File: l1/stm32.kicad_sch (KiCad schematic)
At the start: 9 parts, among them J4 Conn_01x04, SW1 SW_Push, U3 STM32G031K8Tx, Y1 32KHz768

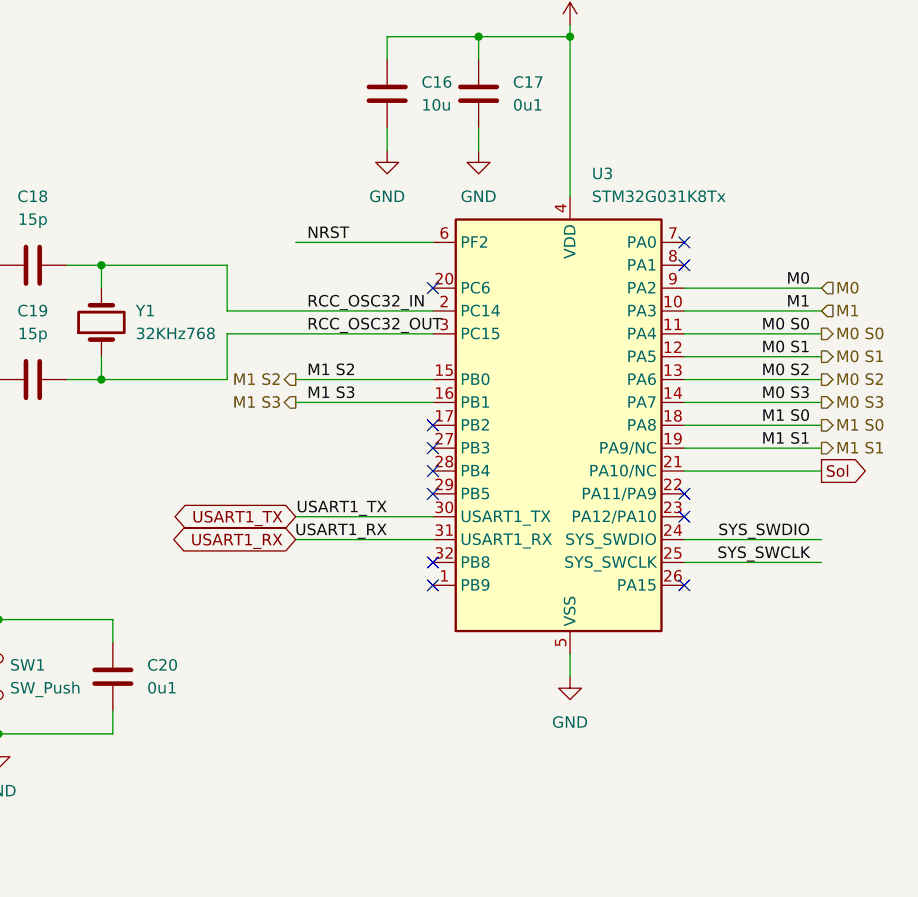
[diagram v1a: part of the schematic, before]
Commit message: Changed To G071
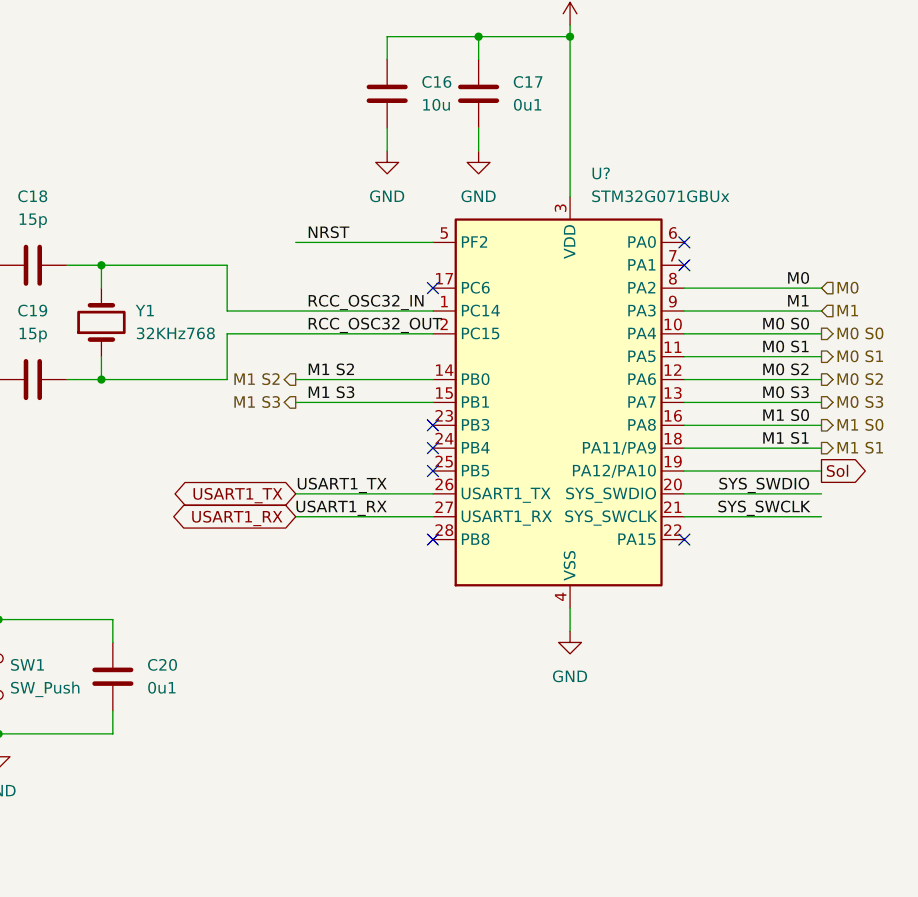
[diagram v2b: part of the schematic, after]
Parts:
- removed U3: STM32G031K8Tx, Package_QFP:LQFP-32_7x7mm_P0.8mm, symbol MCU_ST_STM32G0:STM32G031K8Tx
- added U?: STM32G071GBUx, Package_DFN_QFN:QFN-28_4x4mm_P0.5mm, symbol MCU_ST_STM32G0:STM32G071GBUx
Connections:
- net +3V3: now also U?.3 (VDD)
- net GND: now also U?.4 (VSS)
- net M0: now also U?.8 (PA2)
- net M0 S0: now also U?.10 (PA4)
- net M0 S1: now also U?.11 (PA5)
- net M0 S2: now also U?.12 (PA6)
- net M0 S3: now also U?.13 (PA7)
- net M1: now also U?.9 (PA3)
- net M1 S0: now also U?.16 (PA8)
- net M1 S1: now also U?.18 (PA11/PA9)
- net M1 S2: now also U?.14 (PB0)
- net M1 S3: now also U?.15 (PB1)
- net NRST: now also U?.5 (PF2)
- net RCC_OSC32_IN: now also U?.1 (PC14)
- net RCC_OSC32_OUT: now also U?.2 (PC15)
- net SYS_SWCLK: now also U?.21 (PA14)
- net SYS_SWDIO: now also U?.20 (PA13)
- net Sol: now also U?.19 (PA12/PA10)
- net USART1_RX: now also U?.27 (PB7)
- net USART1_TX: now also U?.26 (PB6)
- no-connect marks 12 -> 8

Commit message: Changed To OKL
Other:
- moved on the sheet: C16, C17, C18, C19, C20, SW1, U?, Y1

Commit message: rough ideation
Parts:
- gave numbers to parts that had none: 1
- renumbered C16 to C201, C17 to C202, C18 to C203, C19 to C204, C20 to C205, J4 to J201, SW1 to SW201, Y1 to Y201
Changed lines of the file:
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@@
 		(dnp no)
 		(fields_autoplaced yes)
-		(property "Reference" "Y1"
+		(property "Reference" "Y201"
 			(at 109.22 92.7099 90)
 			(effects
@@
 			(project "l1"
 				(path "/0e4ddce5-5c0a-41d1-ab67-e7bad6d98362/a63fbca6-593f-4a72-9162-84fa58a2299a/c12d892e-3e71-42fb-9089-506a5d8b9a04"
-					(reference "Y1")
+					(reference "Y201")
 					(unit 1)
 				)
@@
 		(dnp no)
 		(fields_autoplaced yes)
-		(property "Reference" "#PWR030"
+		(property "Reference" "#PWR07"
 			(at 59.69 123.19 0)
 			(effects
@@
 			(project "l1"
 				(path "/0e4ddce5-5c0a-41d1-ab67-e7bad6d98362/a63fbca6-593f-4a72-9162-84fa58a2299a/c12d892e-3e71-42fb-9089-506a5d8b9a04"
-					(reference "#PWR030")
+					(reference "#PWR07")
 					(unit 1)
 				)
@@
 		(dnp no)
 		(fields_autoplaced yes)
-		(property "Reference" "U?"
+		(property "Reference" "U201"
 			(at 159.8232 77.47 0)
 			(effects
@@
 			(project "l1"
 				(path "/0e4ddce5-5c0a-41d1-ab67-e7bad6d98362/a63fbca6-593f-4a72-9162-84fa58a2299a/c12d892e-3e71-42fb-9089-506a5d8b9a04"
-					(reference "U?")
+					(reference "U201")
 					(unit 1)
 				)
@@
 		(dnp no)
 		(fields_autoplaced yes)
-		(property "Reference" "#PWR028"
+		(property "Reference" "#PWR06"
 			(at 82.55 93.98 0)
 			(effects
@@
 			(project "l1"
 				(path "/0e4ddce5-5c0a-41d1-ab67-e7bad6d98362/a63fbca6-593f-4a72-9162-84fa58a2299a/c12d892e-3e71-42fb-9089-506a5d8b9a04"
-					(reference "#PWR028")
+					(reference "#PWR06")
 					(unit 1)
 				)
@@
 		(dnp no)
 		(fields_autoplaced yes)
-		(property "Reference" "C20"
+		(property "Reference" "C205"
 			(at 76.2 107.9499 0)
 			(effects
@@
 			(project "l1"
 				(path "/0e4ddce5-5c0a-41d1-ab67-e7bad6d98362/a63fbca6-593f-4a72-9162-84fa58a2299a/c12d892e-3e71-42fb-9089-506a5d8b9a04"
-					(reference "C20")
+					(reference "C205")
 					(unit 1)
 				)
@@
 		(dnp no)
 		(fields_autoplaced yes)
-		(property "Reference" "#PWR032"
+		(property "Reference" "#PWR010"
 			(at 60.96 157.48 0)
 			(effects
@@
 			(project "l1"
 				(path "/0e4ddce5-5c0a-41d1-ab67-e7bad6d98362/a63fbca6-593f-4a72-9162-84fa58a2299a/c12d892e-3e71-42fb-9089-506a5d8b9a04"
-					(reference "#PWR032")
+					(reference "#PWR010")
 					(unit 1)
 				)
@@
 		(dnp no)
 		(fields_autoplaced yes)
-		(property "Reference" "#PWR031"
+		(property "Reference" "#PWR09"
 			(at 60.96 142.24 0)
 			(effects
@@
 			(project "l1"
 				(path "/0e4ddce5-5c0a-41d1-ab67-e7bad6d98362/a63fbca6-593f-4a72-9162-84fa58a2299a/c12d892e-3e71-42fb-9089-506a5d8b9a04"
-					(reference "#PWR031")
+					(reference "#PWR09")
 					(unit 1)
 				)
@@
 		(dnp no)
 		(fields_autoplaced yes)
-		(property "Reference" "#PWR027"
+		(property "Reference" "#PWR05"
 			(at 147.32 81.28 0)
 			(effects
@@
 			(project "l1"
 				(path "/0e4ddce5-5c0a-41d1-ab67-e7bad6d98362/a63fbca6-593f-4a72-9162-84fa58a2299a/c12d892e-3e71-42fb-9089-506a5d8b9a04"
-					(reference "#PWR027")
+					(reference "#PWR05")
 					(unit 1)
 				)
@@
 		(dnp no)
 		(fields_autoplaced yes)
-		(property "Reference" "#PWR025"
+		(property "Reference" "#PWR03"
 			(at 157.48 64.77 0)
 			(effects
@@
 			(project "l1"
 				(path "/0e4ddce5-5c0a-41d1-ab67-e7bad6d98362/a63fbca6-593f-4a72-9162-84fa58a2299a/c12d892e-3e71-42fb-9089-506a5d8b9a04"
-					(reference "#PWR025")
+					(reference "#PWR03")
 					(unit 1)
 				)
@@
 		(dnp no)
 		(fields_autoplaced yes)
-		(property "Reference" "J4"
+		(property "Reference" "J201"
 			(at 53.34 134.62 0)
 			(effects
@@
 			(project "l1"
 				(path "/0e4ddce5-5c0a-41d1-ab67-e7bad6d98362/a63fbca6-593f-4a72-9162-84fa58a2299a/c12d892e-3e71-42fb-9089-506a5d8b9a04"
-					(reference "J4")
+					(reference "J201")
 					(unit 1)
 				)
@@
 		(dnp no)
 		(fields_autoplaced yes)
-		(property "Reference" "#PWR029"
+		(property "Reference" "#PWR08"
 			(at 157.48 134.62 0)
 			(effects
@@
 			(project "l1"
 				(path "/0e4ddce5-5c0a-41d1-ab67-e7bad6d98362/a63fbca6-593f-4a72-9162-84fa58a2299a/c12d892e-3e71-42fb-9089-506a5d8b9a04"
-					(reference "#PWR029")
+					(reference "#PWR08")
 					(unit 1)
 				)
@@
 		(dnp no)
 		(fields_autoplaced yes)
-		(property "Reference" "C16"
+		(property "Reference" "C201"
 			(at 140.97 67.3099 0)
 			(effects
@@
 			(project "l1"
 				(path "/0e4ddce5-5c0a-41d1-ab67-e7bad6d98362/a63fbca6-593f-4a72-9162-84fa58a2299a/c12d892e-3e71-42fb-9089-506a5d8b9a04"
-					(reference "C16")
+					(reference "C201")
 					(unit 1)
 				)
@@
 		(dnp no)
 		(fields_autoplaced yes)
-		(property "Reference" "C18"
+		(property "Reference" "C203"
 			(at 97.79 80.01 90)
 			(effects
@@
 			(project "l1"
 				(path "/0e4ddce5-5c0a-41d1-ab67-e7bad6d98362/a63fbca6-593f-4a72-9162-84fa58a2299a/c12d892e-3e71-42fb-9089-506a5d8b9a04"
-					(reference "C18")
+					(reference "C203")
 					(unit 1)
 				)
@@
 		(dnp no)
 		(fields_autoplaced yes)
-		(property "Reference" "SW1"
+		(property "Reference" "SW201"
 			(at 60.96 107.9499 90)
 			(effects
@@
 			(project "l1"
 				(path "/0e4ddce5-5c0a-41d1-ab67-e7bad6d98362/a63fbca6-593f-4a72-9162-84fa58a2299a/c12d892e-3e71-42fb-9089-506a5d8b9a04"
-					(reference "SW1")
+					(reference "SW201")
 					(unit 1)
 				)
@@
 		(dnp no)
 		(fields_autoplaced yes)
-		(property "Reference" "C19"
+		(property "Reference" "C204"
 			(at 97.79 92.71 90)
 			(effects
@@
 			(project "l1"
 				(path "/0e4ddce5-5c0a-41d1-ab67-e7bad6d98362/a63fbca6-593f-4a72-9162-84fa58a2299a/c12d892e-3e71-42fb-9089-506a5d8b9a04"
-					(reference "C19")
+					(reference "C204")
 					(unit 1)
 				)
@@
 		(dnp no)
 		(fields_autoplaced yes)
-		(property "Reference" "C17"
+		(property "Reference" "C202"
 			(at 151.13 67.3099 0)
 			(effects
@@
 			(project "l1"
 				(path "/0e4ddce5-5c0a-41d1-ab67-e7bad6d98362/a63fbca6-593f-4a72-9162-84fa58a2299a/c12d892e-3e71-42fb-9089-506a5d8b9a04"
-					(reference "C17")
+					(reference "C202")
 					(unit 1)
 				)
@@
 		(dnp no)
 		(fields_autoplaced yes)
-		(property "Reference" "#PWR026"
+		(property "Reference" "#PWR04"
 			(at 137.16 81.28 0)
 			(effects
@@
 			(project "l1"
 				(path "/0e4ddce5-5c0a-41d1-ab67-e7bad6d98362/a63fbca6-593f-4a72-9162-84fa58a2299a/c12d892e-3e71-42fb-9089-506a5d8b9a04"
-					(reference "#PWR026")
-					(unit 1)
-				)
+					(reference "#PWR04")
+					(unit 1)
+				)

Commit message: 死
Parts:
- removed C201: 10u, Library:cap0603, symbol Device:C
- removed C202, C205: 0u1, Library:cap0603, symbol Device:C
- removed C203, C204: 15p, Library:cap0603, symbol Device:C
- removed J201: Conn_01x04, Connector_JST:JST_XH_S4B-XH-A_1x04_P2.50mm_Horizontal, symbol Connector_Generic:Conn_01x04
- removed SW201: SW_Push, Jumper:SolderJumper-2_P1.3mm_Open_TrianglePad1.0x1.5mm, symbol Switch:SW_Push
- removed U201: STM32G071GBUx, Package_DFN_QFN:QFN-28_4x4mm_P0.5mm, symbol MCU_ST_STM32G0:STM32G071GBUx
- removed Y201: 32KHz768, Crystal:Crystal_SMD_3215-2Pin_3.2x1.5mm, symbol Device:Crystal
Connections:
- no-connect marks 8 -> 0

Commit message: 死
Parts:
- added C203: 2u2, Library:cap0603, symbol Device:C
- added C204, C205, C206, C207, C208: 0u1, Library:cap0603, symbol Device:C
- added D201: RED, Library:led0603, symbol Device:LED
- added R201: R, Library:res0603, symbol Device:R
- added R202: 1K, Library:res0603, symbol Device:R
- added U201: STM32F103CBTX, Package_QFP:LQFP-48_7x7mm_P0.5mm, symbol vincent:STM32F103CBTX
- added Y201: 8Mhz, Crystal:Resonator_SMD_Murata_CSTxExxV-3Pin_3.0x1.1mm, symbol Device:Crystal_GND3
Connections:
- new net: D201.1 (K), R202.1
- new net +3V3 FILT: C203.1, C204.1, C205.1, C206.1, C207.1, C208.1, U201.1 (VBAT), U201.24 (VDD), U201.36 (VDD), U201.48 (VDD), U201.9 (VDDA)
- new net GNDREF: C203.2, C204.2, C205.2, C206.2, C207.2, C208.2, R201.1, R202.2, U201.23 (VSS), U201.35 (VSS), U201.47 (VSS), U201.8 (VSSA), Y201.3
- new net LED DIM: U201.10 (PA0)
- new net LED RX: U201.13 (PA3)
- new net LED TX: U201.12 (PA2)
- new net M1: U201.16 (PA6)
- new net M1 S0: U201.20 (PB2)
- new net M1 S1: U201.21 (PB10)
- new net M1 S2: U201.18 (PB0)
- new net M1 S3: U201.17 (PA7)
- new net M2: U201.19 (PB1)
- new net M2 S0: U201.42 (PB6)
- new net M2 S1: U201.43 (PB7)
- new net M2 S2: U201.41 (PB5)
- new net M2 S3: U201.40 (PB4)
- new net MCU BOOT0: R201.2, U201.44 (BOOT0)
- new net MCU RST: U201.7 (NRST)
- new net MCU SWCLK: U201.37 (PA14)
- new net MCU SWDIO: U201.34 (PA13)
- new net MCU1 LED: D201.2 (A), U201.28 (PB15)
- new net MCU1 OSC IN: U201.5 (PD0), Y201.1
- new net MCU1 OSC OUT: U201.6 (PD1), Y201.2
- no-connect marks 0 -> 20

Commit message: 死
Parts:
- removed U201: STM32F103CBTX, Package_QFP:LQFP-48_7x7mm_P0.5mm, symbol vincent:STM32F103CBTX
- added U301: STM32F103CBTX, Package_DFN_QFN:QFN-48-1EP_7x7mm_P0.5mm_EP5.6x5.6mm, symbol vincent:STM32F103CBTX
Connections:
- net +3V3 FILT: now also U301.1 (VBAT), U301.24 (VDD), U301.36 (VDD), U301.48 (VDD), U301.9 (VDDA)
- net GNDREF: now also U301.23 (VSS), U301.35 (VSS), U301.47 (VSS), U301.8 (VSSA)
- net LED DIM: now also U301.10 (PA0)
- net LED RX: now also U301.13 (PA3)
- net LED TX: now also U301.12 (PA2)
- net M1: now also U301.16 (PA6)
- net M1 S0: now also U301.20 (PB2)
- net M1 S1: now also U301.21 (PB10)
- net M1 S2: now also U301.18 (PB0)
- net M1 S3: now also U301.17 (PA7)
- net M2: now also U301.19 (PB1)
- net M2 S0: now also U301.42 (PB6)
- net M2 S1: now also U301.43 (PB7)
- net M2 S2: now also U301.41 (PB5)
- net M2 S3: now also U301.40 (PB4)
- net MCU BOOT0: now also U301.44 (BOOT0)
- net MCU RST: now also U301.7 (NRST)
- net MCU SWCLK: now also U301.37 (PA14)
- net MCU SWDIO: now also U301.34 (PA13)
- net MCU1 LED: now also U301.28 (PB15)
- net MCU1 OSC IN: now also U301.5 (PD0)
- net MCU1 OSC OUT: now also U301.6 (PD1)

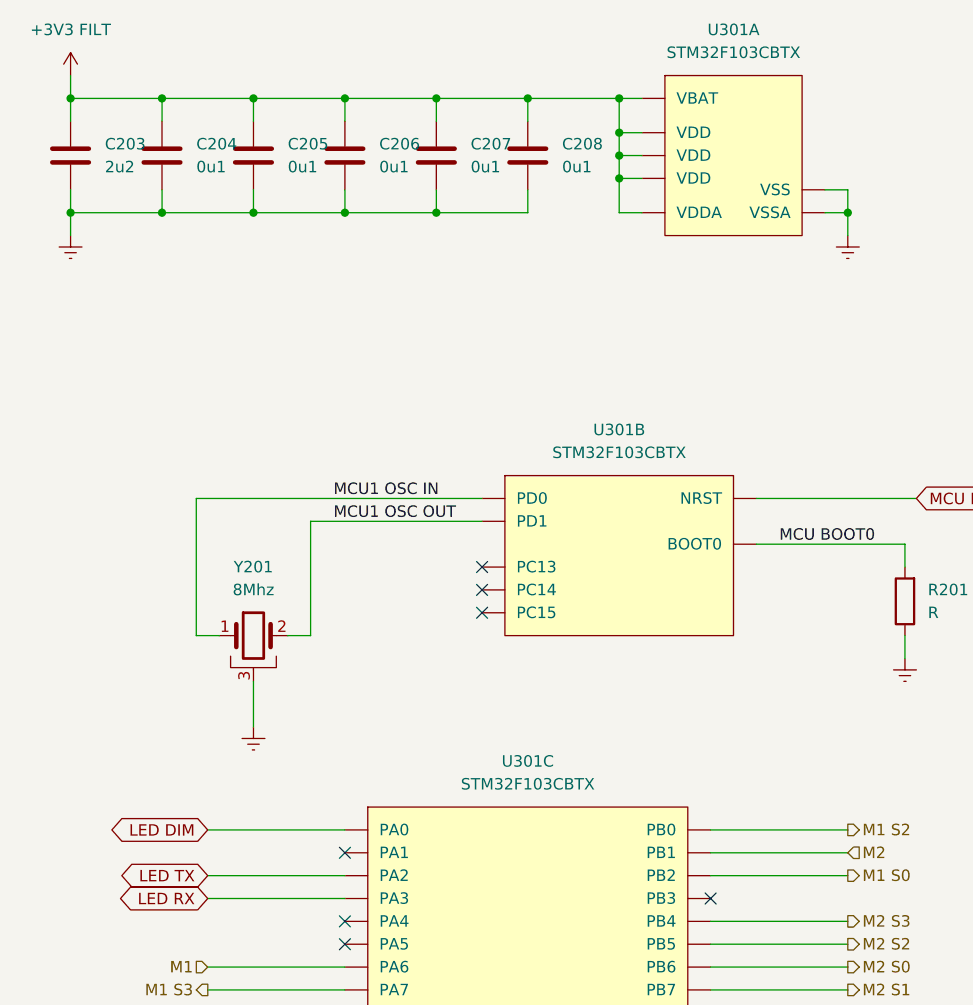
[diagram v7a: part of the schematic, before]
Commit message: Going to move to VNH
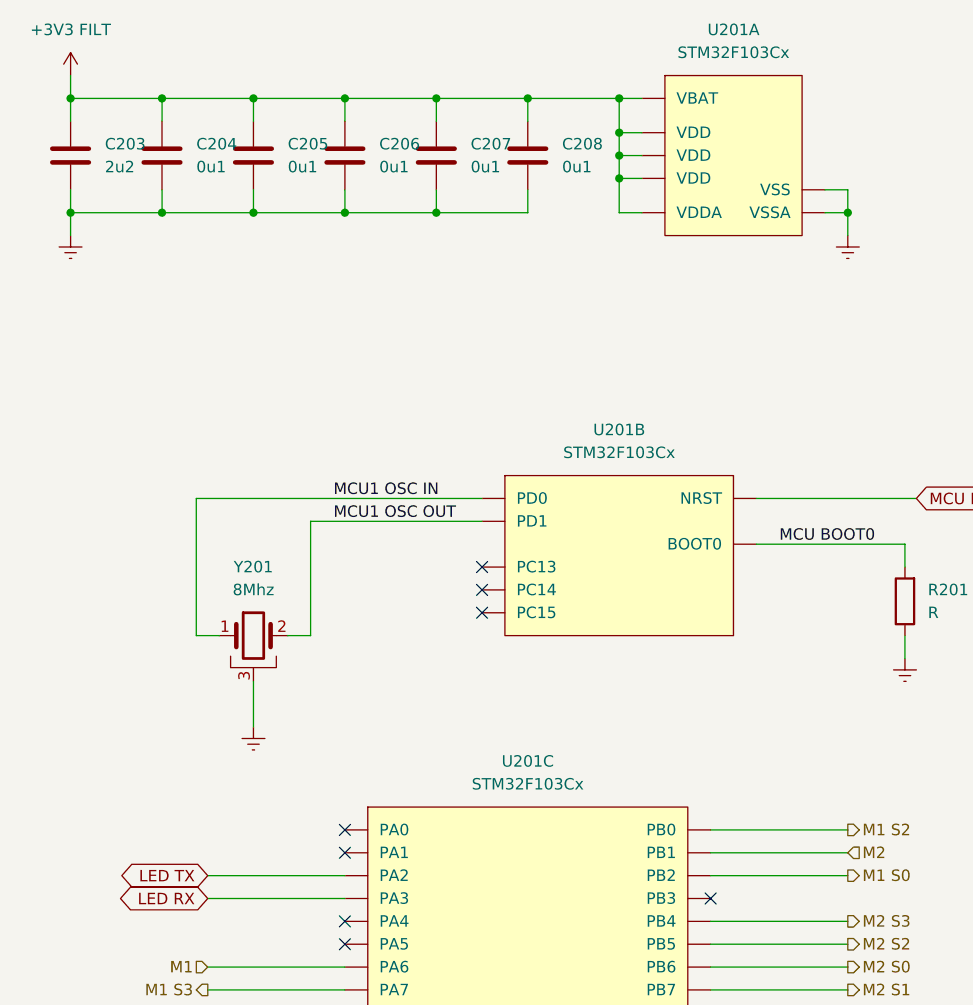
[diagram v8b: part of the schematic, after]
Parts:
- removed U301: STM32F103CBTX, Package_DFN_QFN:QFN-48-1EP_7x7mm_P0.5mm_EP5.6x5.6mm, symbol vincent:STM32F103CBTX
- added U201: STM32F103Cx, Package_DFN_QFN:QFN-48-1EP_7x7mm_P0.5mm_EP5.6x5.6mm_ThermalVias, symbol vincent:STM32F103Cx
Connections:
- net +3V3 FILT: now also U201.1 (VBAT), U201.24 (VDD), U201.36 (VDD), U201.48 (VDD), U201.9 (VDDA)
- net GNDREF: now also U201.23 (VSS), U201.35 (VSS), U201.47 (VSS), U201.49 (EP), U201.8 (VSSA)
- net LED RX: now also U201.13 (PA3)
- net LED TX: now also U201.12 (PA2)
- net M1: now also U201.16 (PA6)
- net M1 S0: now also U201.20 (PB2)
- net M1 S1: now also U201.21 (PB10)
- net M1 S2: now also U201.18 (PB0)
- net M1 S3: now also U201.17 (PA7)
- net M2: now also U201.19 (PB1)
- net M2 S0: now also U201.42 (PB6)
- net M2 S1: now also U201.43 (PB7)
- net M2 S2: now also U201.41 (PB5)
- net M2 S3: now also U201.40 (PB4)
- net MCU BOOT0: now also U201.44 (BOOT0)
- net MCU RST: now also U201.7 (NRST)
- net MCU SWCLK: now also U201.37 (PA14)
- net MCU SWDIO: now also U201.34 (PA13)
- net MCU1 LED: now also U201.28 (PB15)
- net MCU1 OSC IN: now also U201.5 (PD0)
- net MCU1 OSC OUT: now also U201.6 (PD1)
- no-connect marks 20 -> 21
